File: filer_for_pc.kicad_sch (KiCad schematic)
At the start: 84 parts, among them J1 Ethernet In, J2 Ethernet Out

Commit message: Upgrade
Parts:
- removed C19: 3 mkF, symbol Device:C
- removed C22, C23, C3, C7: C,IEC, symbol PCM_Generic:C,IEC
- removed C26, C30: C, 100 nF, symbol PCM_Generic:C,IEC
- removed C27, C28, C31, C32: C, 22 pF, symbol PCM_Generic:C,IEC
- removed R12: 1 Om, symbol Device:R_Small
- removed R16: 33 kOm, symbol Device:R_Small
- removed R2, R26, R27, R6, R9: R,IEC, symbol PCM_Generic:R,IEC
- removed R29, R30: R, 90 Om, symbol PCM_Generic:R,IEC
- removed R31, R32, R33, R7: R, 10 Om, symbol PCM_Generic:R,IEC
- added C22, C37: 100 nF, symbol Device:C
- added C23, C36: 10 nF, symbol Device:C
- added C24, C25: 1 mkF, symbol Device:C
- added C26, C35: 1 nF, symbol Device:C
- added C27, C34: 820 pF, symbol Device:C
- added C28, C33: 220 pF, symbol Device:C
- added C3, C40, C41: 5.6 mkF Audiofiler+, symbol Device:C
- added C30, C32: 100 pF, symbol Device:C
- added C31, C39: 22 pF, symbol Device:C
- added C38, C7: 470 nF, symbol Device:C
- added R17, R18, R19, R20, R22, R25, R26, R27: 2 Om, symbol Device:R
- added R2, R21, R23, R24, R28, R29, R6, R7, R9: 1 Om, symbol Device:R
- added R30, R31: 1-2 kOm, symbol Device:R
- C18: value Set of capasitors from 10 mkF to 1 nF -> Set of capasitors from 10 mkF to 22 pF
- L10: value 70 turns on ferrite core -> I use ~70 turns of wire but same coil as "emmiter" beter
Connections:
- net out: now also C25.1, C25.2
- net at L1.1 (+): now also C3.2, C32.1, C33.1, C34.1, C35.1, C36.1, C37.1, C38.1, C39.1
- net at L2.1 (+): now also C22.1, C23.1, C26.1, C27.1, C28.1, C30.1, C31.1, C40.2, C7.1
- net 220 V or Line: now reaches L10.1
- net at C15.2, L7.4, L8.1: now also C24.1
- net at C10.1, L7.3, L8.2: now also C24.2
- net GND: no longer names the net of L2.2 (-)
- net GND: now also C3.1, R17.2, R18.2, R19.2, R2.2, R20.2, R30.2, R31.1, R6.2, R7.2, R9.2; no longer L1.2 (-)
- new net: C26.2, R18.1
- new net: C22.2, R20.1
- new net: C38.2, R28.1
- new net: C36.2, R26.1
- new net: C35.2, R25.1
- new net: C23.2, R19.1
- new net: C7.2, R9.1
- new net: C27.2, R7.1
- new net: C28.2, R6.1
- new net: C34.2, R24.1
- new net: C32.2, R22.1
- new net: C40.1, C41.1, R29.1, R30.1
- new net: C39.2, R21.1
- new net: C33.2, R23.1
- new net: C30.2, R17.1
- new net: C37.2, R27.1
- new net: C31.2, R2.1
- new net GNDS: C41.2, L1.2 (-), R21.2, R22.2, R23.2, R24.2, R25.2, R26.2, R27.2, R28.2, R31.2
- new net input: R29.2
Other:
- note removed: "To much times hacked just use all possible filters for sound"
- moved on the sheet: L1, L2

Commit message: Upgrade
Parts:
- L10: value I use ~70 turns of wire but same coil as "emmiter" beter -> I use ~70 turns of wire on ferrite
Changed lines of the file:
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@@
 			)
 		)
-		(property "Value" "I use ~70 turns of wire but same coil as \"emmiter\" beter"
-			(at 98.806 113.538 0)
+		(property "Value" "I use ~70 turns of wire on ferrite"
+			(at 115.57 111.506 0)
 			(effects
 				(font

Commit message: Upgrade
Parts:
- removed L10: I use ~70 turns of wire on ferrite, symbol Device:L
- removed LS1: 100+ Om speaker, symbol Device:Speaker
- added C19, C43, C47: 100 nF, symbol Device:C
- added C42, C46: 1 nF, symbol Device:C
- added C44, C48: 10 nF, symbol Device:C
- added C45, C49, C55, C56: 1 mkF, symbol Device:C
- added C50, C51, C52, C53, C54: 2.2 nF, symbol Device:C
- added RV1: ~240 V, symbol Device:Varistor
- C18: value Set of capasitors from 10 mkF to 22 pF -> 10 nF
- C24: value 1 mkF -> 1 nF
- L7, L8: value 30-50 turns -> 10-15 turns
- L9: value 30-50 turns -> 20-30 turns
- R11: value 100 kOm -> 1 Om
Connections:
- net GNDS: now also R17.2, R18.2, R19.2, R2.2, R20.2, R30.2, R6.2, R7.2, R9.2
- net in: now also C53.2, C54.1
- net out: now also C18.1, C18.2, C19.1, C19.2, C42.1, C42.2, C52.1, C52.2, C55.1, C56.1, RV1.1, RV1.2
- net at C14.2, L8.4, L9.1: now also C24.1, C43.1, C44.1, C45.1, C50.1, C56.2
- net at C11.1, L8.3, L9.2: now also C24.2, C43.2, C44.2, C45.2, C50.2, C55.2
- net at R11.1: now also C53.1, C54.2
- net at C15.2, L7.4, L8.1: now also C46.2, C47.2, C48.2, C49.2, C51.2; no longer C24.1
- net at C10.1, L7.3, L8.2: now also C51.1; no longer C24.2
- new net: C46.1, C47.1, C48.1, C49.1
- new net: C3.1, L2.2 (-), R31.1
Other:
- note removed: "Wind generator"
- moved on the sheet: C25

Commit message: Update .....
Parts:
- removed C41: 5.6 mkF Audiofiler+, symbol Device:C
- removed R29: 1 Om, symbol Device:R
- removed R30, R31: 1-2 kOm, symbol Device:R
- added D17, D18: 12v, symbol Device:D_Zener
- renumbered C1 to C6, C1 to C8
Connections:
- net GNDS: now also D17.2 (A)
- net input: now also C40.1
- net at C3.2, C32.1, C33.1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: now also D17.1 (K)
- net at C22.1, C23.1, C26.1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: now also D18.1 (K)
- net at C3.1, L2.2 (-): now also D18.2 (A)

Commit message: Upgreade
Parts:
- removed C20, C21, C29, C9: ~50uF, symbol PCM_Elektuur:C-polar
- removed D1, D10, D11, D12, D13, D14, D15, D16, D2, D3, D4, D5, D6, D7, D8, D9: D, symbol Device:D
- removed J1: Ethernet In, 4ms_Connector:Pins_1x08_2.54mm_TH, symbol PCM_4ms_Connector:Conn_01x08
- removed J2: Ethernet Out, 4ms_Connector:Pins_1x08_2.54mm_TH, symbol PCM_4ms_Connector:Conn_01x08
- removed R10, R13, R14, R15: 10 Om, symbol PCM_Generic:R,IEC
- added AE3: Antenna, symbol Device:Antenna
- added C20, C21, C58, C9: 100 nF, symbol Device:C
- added C29, C59: C,IEC, symbol PCM_Generic:C,IEC
- added C41, C57: C, symbol Device:C
- added L10, L11: L, symbol Device:L
- added R10, R13, R14, R15: 220 Om, symbol Device:R_Small
- added R12, R16: ~1.8 kOm, symbol Device:R
- added R29: R,IEC, symbol PCM_Generic:R,IEC
- added RV2, RV3, RV4: ~250 V, symbol Device:Varistor
- C3, C40: value 5.6 mkF Audiofiler+ -> 8.2 mkF Audiofiler+
- RV1: value ~240 V -> ~250 V
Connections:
- net GNDS: now also D18.2 (A), R12.2, R16.2
- net Line: now also C29.1 (+)
- net Neutral: now also C59.2 (-)
- net in: now also R14.2, RV4.2; no longer C16.2, C53.2, L7.1
- net input: now also R12.1
- net out: now also C20.1, R13.2
- net at C46.1, C47.1, C48.1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: now also R15.2, RV3.1
- net at C15.2, C46.2, C47.2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: now also C58.1, RV3.2
- net Grounding device 1: now reaches R1.2, R11.2, R5.2
- net Grounding device 1: now also C1.2, C2.2, C4.2, C5.2, C41.2, C57.2; no longer R3.2, R4.2
- net at C14.2, C24.1, C43.1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: now also C9.1, RV2.1
- net at C11.1, C24.2, C43.2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: now also R10.2, RV2.2
- net at L4.1: now also AE1.1 (A), L3.1
- net at L6.1: now also AE2.1 (A), L5.1
- net at C3.1, L2.2 (-): now also R16.1; no longer D18.2 (A)
- new net: C20.2, R13.1
- new net: C21.2, R14.1
- new net: L10.1, L11.1
- new net: C41.1, L10.2
- new net: C29.2 (-), C59.1 (+), R29.1 (+)
- new net: C58.2, R15.1
- new net: C9.2, R10.1
- new net: C57.1, L11.2
- new net Grounding device 2: R3.2, R4.2
- new net in Line: C16.2, C21.1, C53.2, L7.1, RV4.1
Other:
- note added: "0.5 M"
- note added: "0.7 M"
- note added: "28.05.2025"
- note removed: "Anti piracy radio reciver"
- note removed: "For this, pirates turn off the Internet over twisted pair cables and break mobile phones, as well as for firewalls on the computer and on the router, the adaptive ASA firewall seems to have been completely killed"
- moved on the sheet: C4, C43, C44, C45, C47, C48, C49, C5, L5, L6

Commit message: Update
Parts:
- C3, C40: value 8.2 mkF Audiofiler+ -> 8.2 mkF Audio cap
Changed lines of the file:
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@@
 			)
 		)
-		(property "Value" "8.2 mkF Audiofiler+"
+		(property "Value" "8.2 mkF Audio cap"
 			(at 251.46 68.5799 0)
 			(effects
@@
 			)
 		)
-		(property "Value" "8.2 mkF Audiofiler+"
+		(property "Value" "8.2 mkF Audio cap"
 			(at 251.46 100.3299 0)
 			(effects

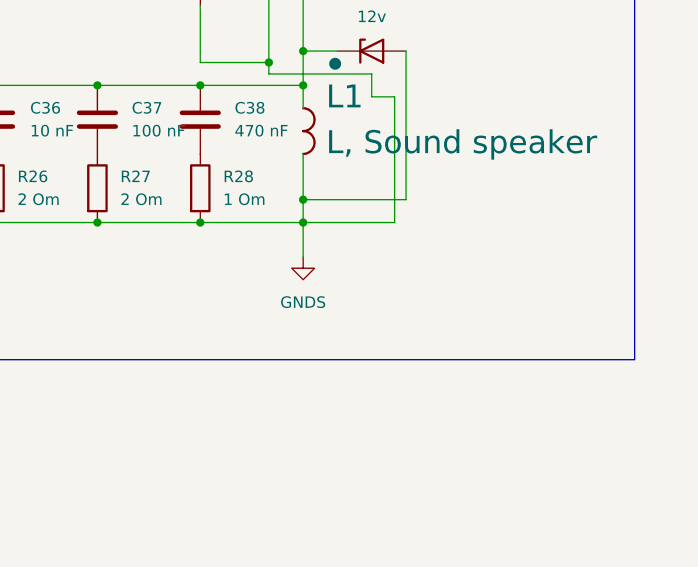
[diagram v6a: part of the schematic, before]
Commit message: Update | RF radiation exposure warning
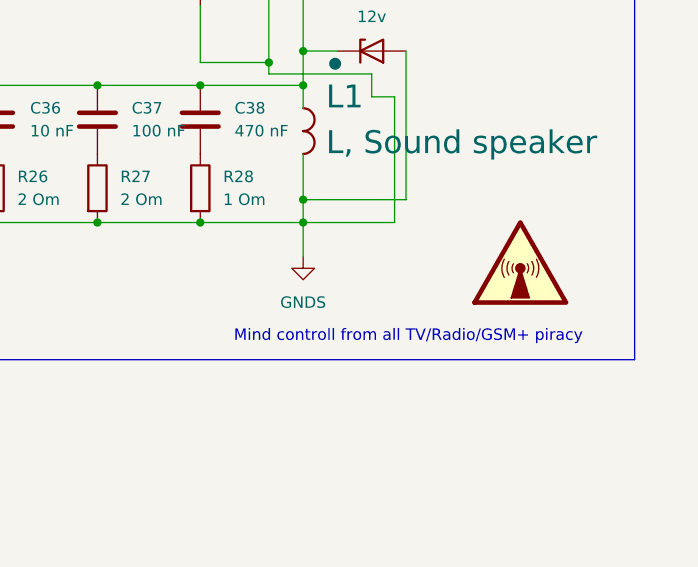
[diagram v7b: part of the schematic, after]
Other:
- note added: "Mind controll from all TV/Radio/GSM+ piracy"
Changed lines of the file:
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@@
 		)
 	)
+	(text "Mind controll from all TV/Radio/GSM+ piracy"
+		(exclude_from_sim no)
+		(at 259.334 140.97 0)
+		(effects
+			(font
+				(size 1.27 1.27)
+			)
+		)
+	)
 	(text "11\n"
 		(exclude_from_sim no)
@@
 					(unit 1)
 				)
+			)
+		)
+	)
+	(symbol
+		(lib_id "Graphic:SYM_Radio_Waves_Large")
+		(at 271.78 132.08 0)
+		(unit 1)
+		(exclude_from_sim no)
+		(in_bom no)
+		(on_board no)
+		(dnp no)
+		(fields_autoplaced yes)
+		(property "Reference" "#SYM1"
+			(at 271.78 127 0)
+			(effects
+				(font
+					(size 1.27 1.27)
+				)
+				(hide yes)
+			)
+		)
+		(property "Value" "SYM_Radio_Waves_Large"
+			(at 271.78 138.43 0)
+			(effects
+				(font
+					(size 1.27 1.27)
+				)
+				(hide yes)
+			)
+		)
+		(property "Footprint" ""
+			(at 271.78 137.16 0)
+			(effects
+				(font
+					(size 1.27 1.27)
+				)
+				(hide yes)
+			)
+		)
+		(property "Datasheet" "~"
+			(at 272.542 137.16 0)
+			(effects
+				(font
+					(size 1.27 1.27)
+				)
+				(hide yes)
+			)
+		)
+		(property "Description" "Radio waves warning symbol, large"
+			(at 271.78 132.08 0)
+			(effects
+				(font
+					(size 1.27 1.27)
+				)
+				(hide yes)
+			)
+		)
+		(property "Sim.Enable" "0"
+			(at 271.78 132.08 0)
+			(effects
+				(font
+					(size 1.27 1.27)
+				)
+				(hide yes)
+			)
+		)
+		(instances
+			(project ""
+				(path "/cdde10a9-1f5d-4493-ba10-a349138f6d4d"
+					(reference "#SYM1")
+					(unit 1)
+				)

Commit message: Update
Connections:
- net input: no longer R12.1
- net at C3.2, C32.1, C33.1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: now also R16.1
- net at C22.1, C23.1, C26.1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: now also R12.1
- net at C3.1, L2.2 (-): no longer R16.1
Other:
- moved on the sheet: R12
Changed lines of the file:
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@@
 	)
 	(junction
+		(at 251.46 109.22)
+		(diameter 0)
+		(color 0 0 0 0)
+	)
+	(junction
 		(at 40.64 116.84)
 		(diameter 0)
@@
 	)
 	(junction
-		(at 247.65 93.98)
-		(diameter 0)
-		(color 0 0 0 0)
-	)
-	(junction
 		(at 90.17 125.73)
 		(diameter 0)
@@
 	)
 	(junction
-		(at 236.22 63.5)
-		(diameter 0)
-		(color 0 0 0 0)
-	)
-	(junction
 		(at 115.57 91.44)
 		(diameter 0)
@@
 	)
 	(junction
+		(at 251.46 71.12)
+		(diameter 0)
+		(color 0 0 0 0)
+	)
+	(junction
 		(at 20.32 116.84)
 		(diameter 0)
@@
 	(wire
 		(pts
-			(xy 247.65 93.98) (xy 247.65 95.25)
+			(xy 247.65 83.82) (xy 247.65 95.25)
 		)
 		(stroke
@@
 	(wire
 		(pts
-			(xy 247.65 83.82) (xy 247.65 93.98)
-		)
-		(stroke
-			(width 0)
-			(type default)
-		)
-	)
-	(wire
-		(pts
-			(xy 247.65 71.12) (xy 256.54 71.12)
+			(xy 247.65 71.12) (xy 251.46 71.12)
 		)
 		(stroke
@@
 	(wire
 		(pts
-			(xy 236.22 63.5) (xy 247.65 63.5)
+			(xy 209.55 63.5) (xy 247.65 63.5)
 		)
 		(stroke
@@
 	(wire
 		(pts
+			(xy 237.49 62.23) (xy 251.46 62.23)
+		)
+		(stroke
+			(width 0)
+			(type default)
+		)
+	)
+	(wire
+		(pts
 			(xy 81.3134 21.59) (xy 81.3134 46.99)
 		)
@@
 	(wire
 		(pts
+			(xy 251.46 62.23) (xy 251.46 71.12)
+		)
+		(stroke
+			(width 0)
+			(type default)
+		)
+	)
+	(wire
+		(pts
 			(xy 66.04 91.44) (xy 66.04 92.71)
 		)
@@
 	(wire
 		(pts
-			(xy 236.22 71.12) (xy 243.84 71.12)
+			(xy 237.49 73.66) (xy 243.84 73.66)
 		)
 		(stroke
@@
 	(wire
 		(pts
-			(xy 209.55 63.5) (xy 236.22 63.5)
+			(xy 236.22 128.27) (xy 247.65 128.27)
 		)
 		(stroke
@@
 	(wire
 		(pts
-			(xy 236.22 128.27) (xy 247.65 128.27)
+			(xy 101.5773 129.54) (xy 95.25 129.54)
 		)
 		(stroke
@@
 	(wire
 		(pts
-			(xy 101.5773 129.54) (xy 95.25 129.54)
+			(xy 237.49 62.23) (xy 237.49 66.04)
 		)
 		(stroke
@@
 	(wire
 		(pts
-			(xy 243.84 71.12) (xy 243.84 90.17)
+			(xy 243.84 73.66) (xy 243.84 90.17)
 		)
 		(stroke
@@
 	(wire
 		(pts
+			(xy 251.46 93.98) (xy 251.46 109.22)
+		)
+		(stroke
+			(width 0)
+			(type default)
+		)
+	)
+	(wire
+		(pts
 			(xy 172.72 113.03) (xy 182.88 113.03)
 		)
@@
 	(wire
 		(pts
+			(xy 236.22 93.98) (xy 251.46 93.98)
+		)
+		(stroke
+			(width 0)
+			(type default)
+		)
+	)
+	(wire
+		(pts
 			(xy 135.89 171.45) (xy 149.86 171.45)
 		)
@@
 	(wire
 		(pts
-			(xy 236.22 93.98) (xy 247.65 93.98)
+			(xy 251.46 71.12) (xy 256.54 71.12)
 		)
 		(stroke
@@
 		(at 271.78 132.08 0)
 		(unit 1)
-		(exclude_from_sim no)
+		(exclude_from_sim yes)
 		(in_bom no)
 		(on_board no)
@@
 			)
 		)
-		(property "Sim.Enable" "0"
-			(at 271.78 132.08 0)
-			(effects
-				(font
-					(size 1.27 1.27)
-				)
-				(hide yes)
-			)
-		)
 		(instances
 			(project ""
@@
 	(symbol
 		(lib_id "Device:R")
-		(at 236.22 67.31 0)
+		(at 237.49 69.85 0)
 		(unit 1)
 		(exclude_from_sim no)
@@
 		(fields_autoplaced yes)
 		(property "Reference" "R12"
-			(at 238.76 66.0399 0)
+			(at 240.03 68.5799 0)
 			(effects
 				(font
@@
 		)
 		(property "Value" "~1.8 kOm"
-			(at 238.76 68.5799 0)
+			(at 240.03 71.1199 0)
 			(effects
 				(font
@@
 		)
 		(property "Footprint" ""
-			(at 234.442 67.31 90)
+			(at 235.712 69.85 90)
 			(effects
 				(font
@@
 		)
 		(property "Datasheet" "~"
-			(at 236.22 67.31 0)
+			(at 237.49 69.85 0)
 			(effects
 				(font
@@
 		)
 		(property "Description" "Resistor"
-			(at 236.22 67.31 0)
+			(at 237.49 69.85 0)
 			(effects
 				(font
